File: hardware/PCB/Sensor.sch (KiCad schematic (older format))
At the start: 2 parts

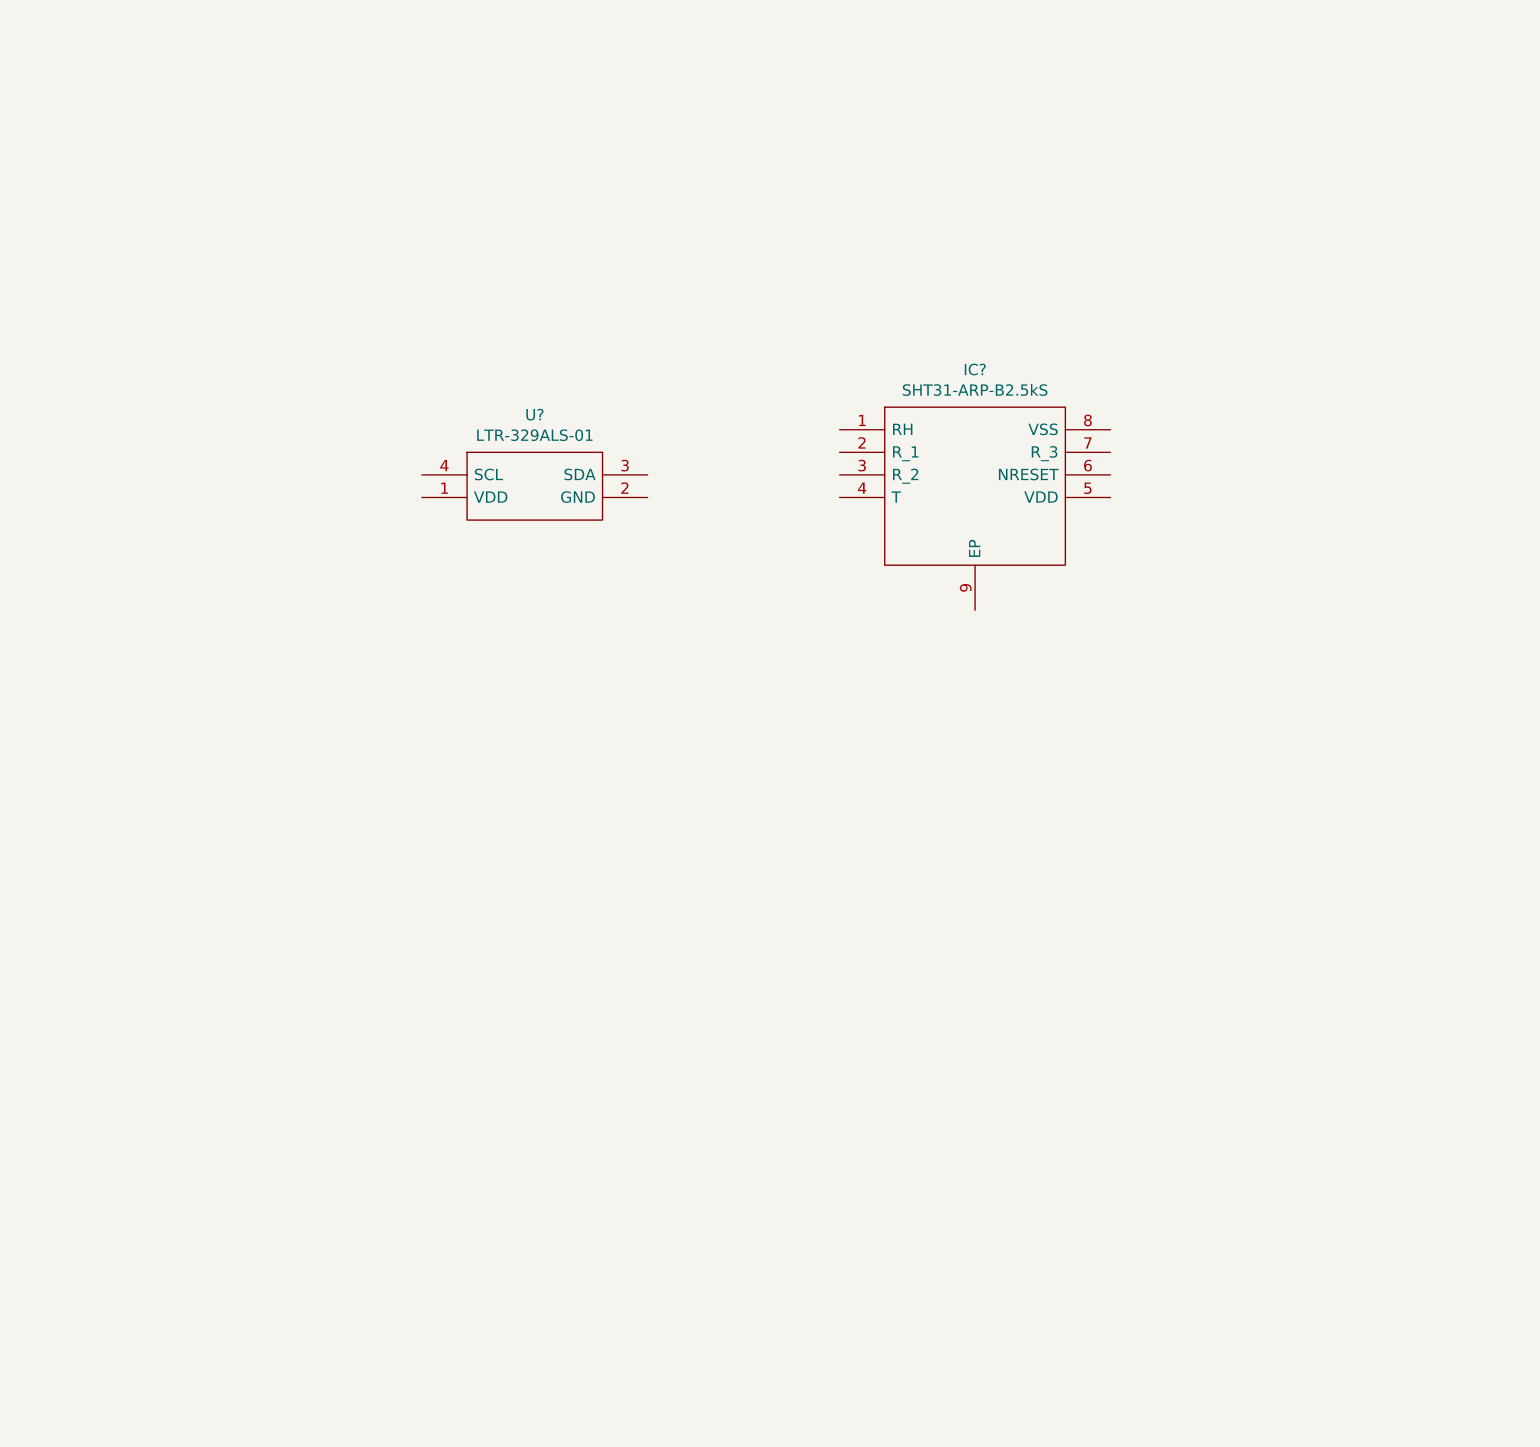
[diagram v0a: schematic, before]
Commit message: Complete Sensor schematic
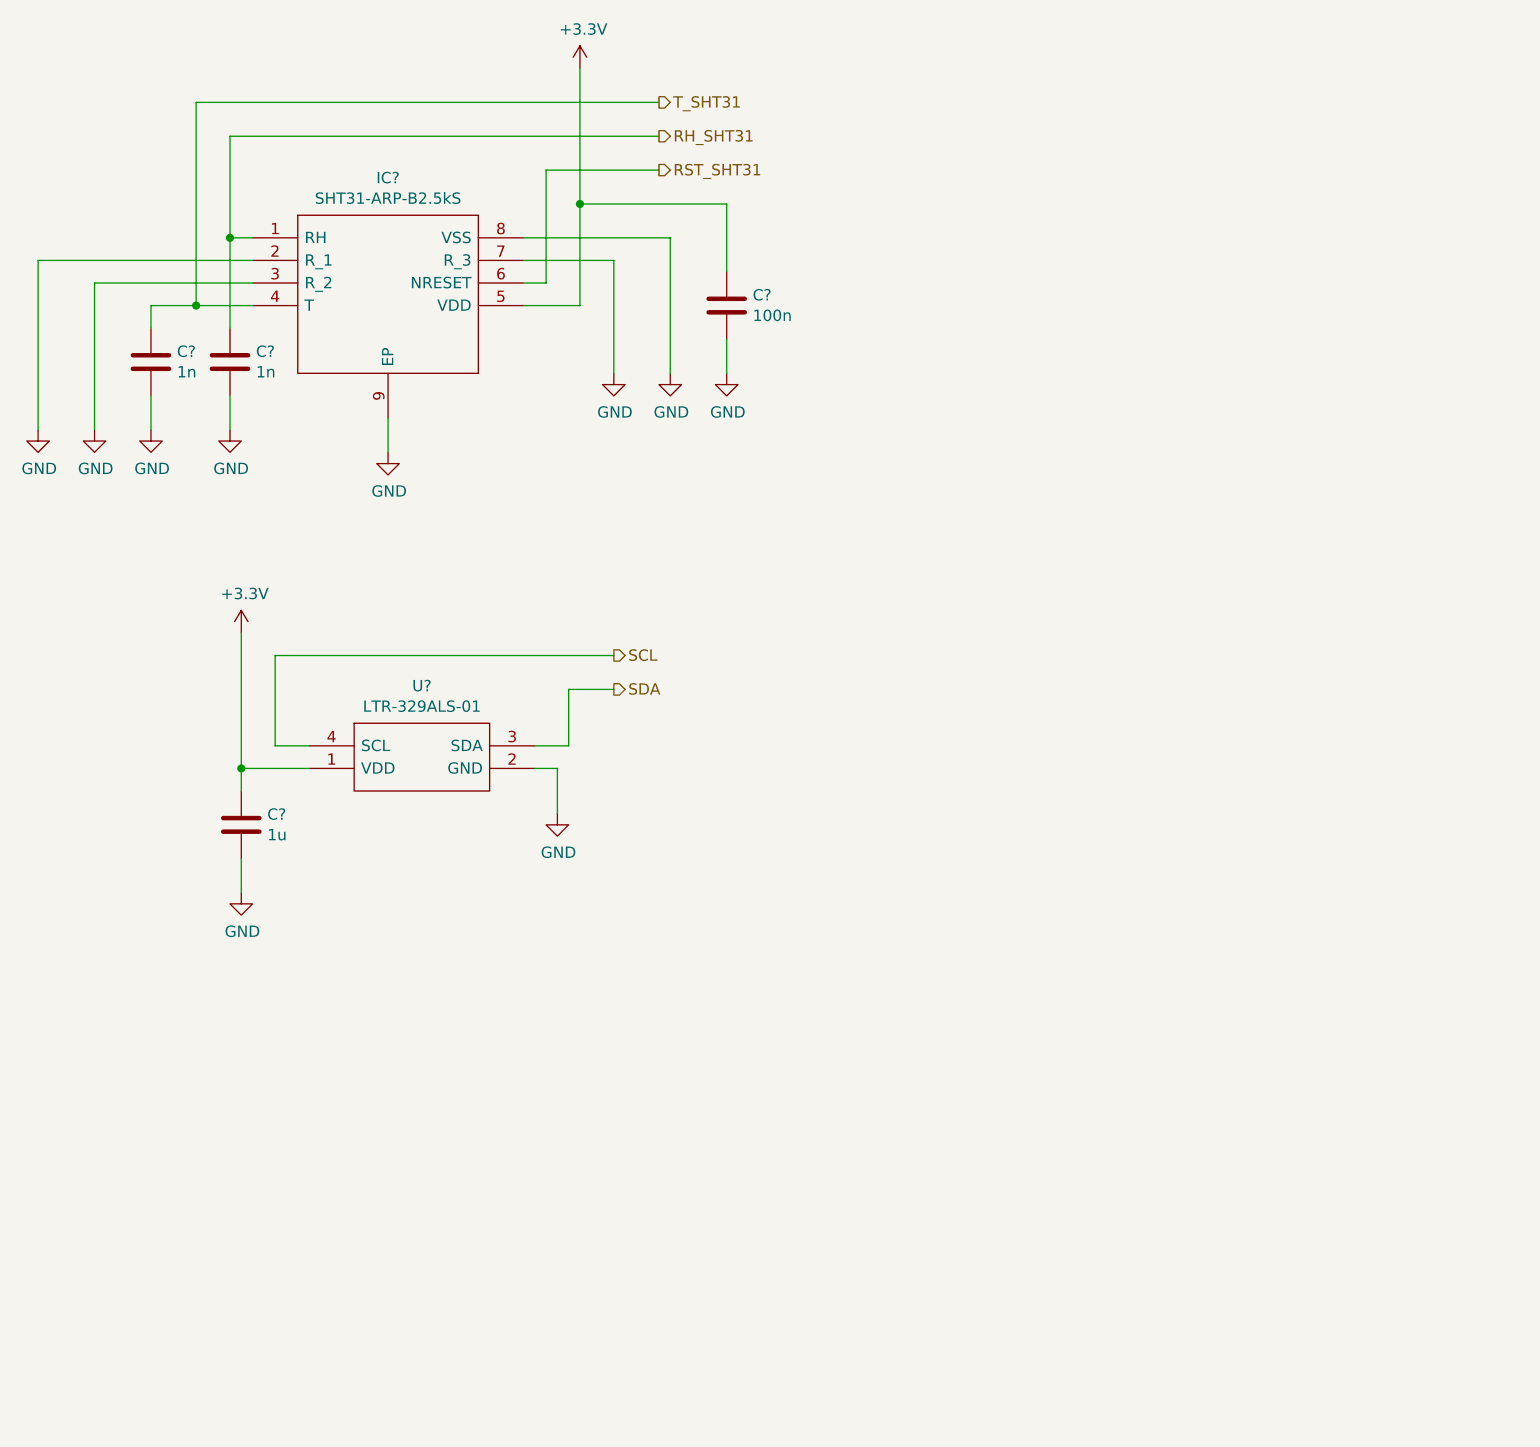
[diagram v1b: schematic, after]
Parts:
- added C?: 100n, symbol Device:C
- added C? (x2): 1n, symbol Device:C
- added C?: 1u, symbol Device:C
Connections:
- net +3V3: now reaches U?.1 (VDD)
- net +3V3: now also IC?.5 (VDD), C?.1, C?.1
- net GND: now reaches U?.2 (GND)
- net GND: now also IC?.2 (R_1), IC?.3 (R_2), IC?.7 (R_3), IC?.8 (VSS), IC?.9 (EP), C?.2, C?.2, C?.2, C?.2
- net SDA: now reaches U?.3 (SDA)
- net SCL: now reaches U?.4 (SCL)
- net RH_SHT31: now reaches IC?.1 (RH)
- net RH_SHT31: now also C?.1
- net T_SHT31: now reaches IC?.4 (T)
- net T_SHT31: now also C?.1
- net RST_SHT31: now reaches IC?.6 (NRESET)
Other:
- moved on the sheet: IC?, U?

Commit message: Add LPS22HD pressure sensor
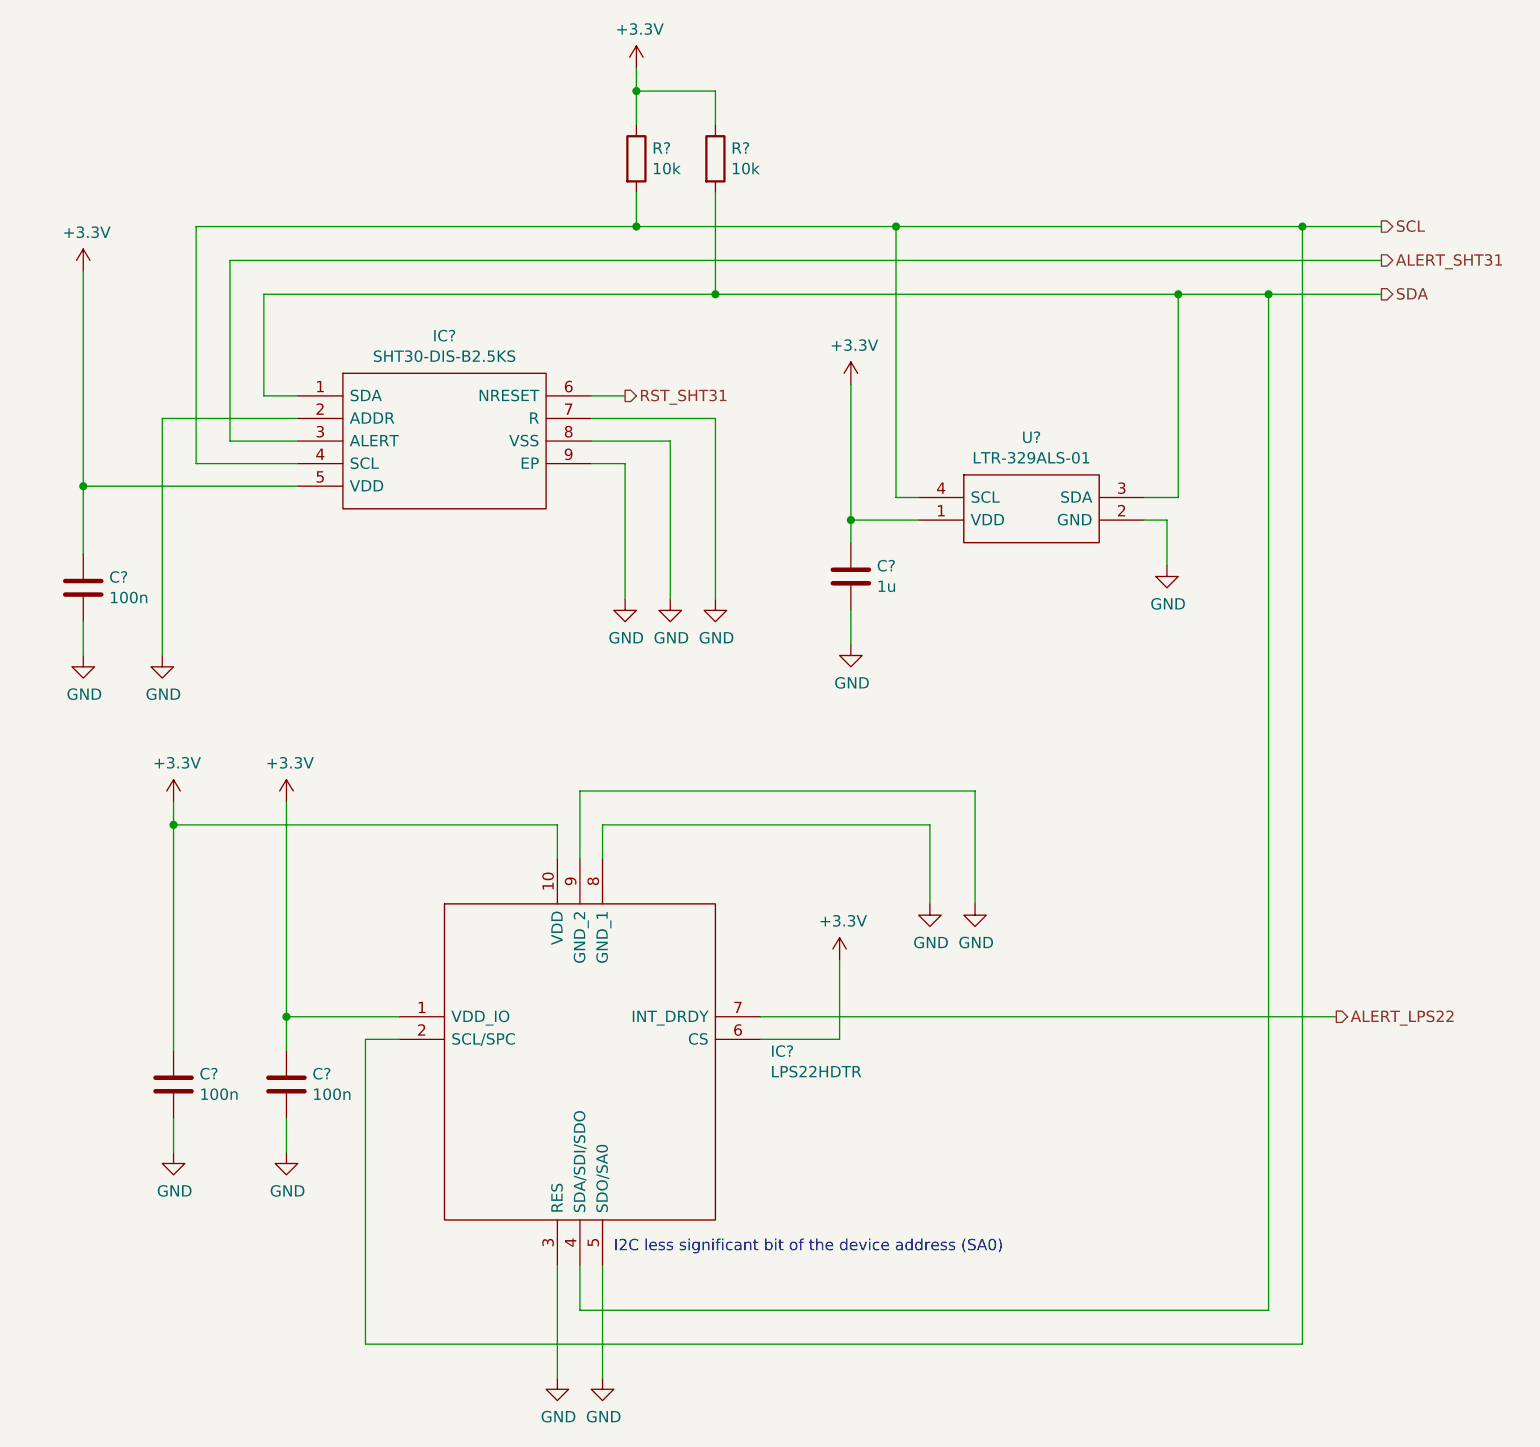
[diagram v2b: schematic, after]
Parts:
- removed C?: 100n, symbol Device:C
- removed C? (x2): 1n, symbol Device:C
- removed IC?: SHT31-ARP-B2.5kS, SON50P250X250X100-9N-D, symbol ProjectLibrary:SHT31-ARP-B2.5kS
- added C? (x3): 100n, symbol Device:C
- added IC?: SHT30-DIS-B2.5KS, SHT30DISB25KS, symbol ProjectLibrary:SHT30-DIS-B2.5KS
- added IC?: LPS22HDTR, LPS22HDTR, symbol ProjectLibrary:LPS22HDTR
- added R? (x2): 10k, symbol Device:R
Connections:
- net +3V3: now also C?.1, C?.1, C?.1, IC?.1 (VDD_IO), IC?.10 (VDD), IC?.5 (VDD), IC?.6 (CS), R?.1, R?.1
- net GND: now also C?.2, C?.2, C?.2, IC?.2 (ADDR), IC?.3 (RES), IC?.5 (SDO/SA0), IC?.7 (R), IC?.8 (GND_1), IC?.8 (VSS), IC?.9 (EP), IC?.9 (GND_2)
- net RST_SHT31: now also IC?.6 (NRESET)
- net SCL: now also IC?.2 (SCL/SPC), IC?.4 (SCL), R?.2
- net SDA: now also IC?.1 (SDA), IC?.4 (SDA/SDI/SDO), R?.2
- new net ALERT_LPS22: IC?.7 (INT_DRDY)
- new net ALERT_SHT31: IC?.3 (ALERT)
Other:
- note added: "I2C less significant bit of the device address (SA0)"
- moved on the sheet: C?, U?

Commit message: add 10k pull up
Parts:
- added R? (x3): 10k, symbol Device:R
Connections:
- net +3V3: now also R?.1, R?.1, R?.1
- net ALERT_LPS22: now also R?.2
- net ALERT_SHT31: now also R?.2
- net RST_SHT31: now also R?.2
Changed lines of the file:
@@
 Text HLabel 3350 2300 2    50   Output ~ 0
 RST_SHT31
-Wire Wire Line
-	3200 2300 3350 2300
 Text HLabel 6700 1550 2    50   Output ~ 0
 SCL
@@
 Connection ~ 4550 1550
 Wire Wire Line
-	4550 1550 6350 1550
-Wire Wire Line
-	1600 1700 6700 1700
+	1600 1700 6200 1700
 Wire Wire Line
 	3750 1850 5800 1850
@@
 ALERT_LPS22
 Wire Wire Line
-	3950 5050 6500 5050
+	3950 5050 5750 5050
+$Comp
+L Device:R R?
+U 1 1 5FD8C795
+P 3100 1250
+F 0 "R?" H 3170 1296 50  0000 L CNN
+F 1 "10k" H 3170 1205 50  0000 L CNN
+F 2 "" V 3030 1250 50  0001 C CNN
+F 3 "~" H 3100 1250 50  0001 C CNN
+	1    3100 1250
+	1    0    0    -1
+$EndComp
+$Comp
+L Device:R R?
+U 1 1 5FD8E1C7
+P 6200 1300
+F 0 "R?" H 6270 1346 50  0000 L CNN
+F 1 "10k" H 6270 1255 50  0000 L CNN
+F 2 "" V 6130 1300 50  0001 C CNN
+F 3 "~" H 6200 1300 50  0001 C CNN
+	1    6200 1300
+	1    0    0    -1
+$EndComp
+$Comp
+L Device:R R?
+U 1 1 5FD8FA02
+P 5750 4800
+F 0 "R?" H 5820 4846 50  0000 L CNN
+F 1 "10k" H 5820 4755 50  0000 L CNN
+F 2 "" V 5680 4800 50  0001 C CNN
+F 3 "~" H 5750 4800 50  0001 C CNN
+	1    5750 4800
+	1    0    0    -1
+$EndComp
+Wire Wire Line
+	4550 1550 6350 1550
+Wire Wire Line
+	3200 2300 3300 2300
+Wire Wire Line
+	3100 950  3400 950
+Wire Wire Line
+	3100 950  3100 1100
+Wire Wire Line
+	3100 1400 3100 2000
+Wire Wire Line
+	3100 2000 3300 2000
+Wire Wire Line
+	3300 2000 3300 2300
+Connection ~ 3300 2300
+Wire Wire Line
+	3300 2300 3350 2300
+Wire Wire Line
+	6200 1450 6200 1700
+Connection ~ 6200 1700
+Wire Wire Line
+	6200 1700 6700 1700
+$Comp
+L power:+3.3V #PWR?
+U 1 1 5FDA12EA
+P 6200 1000
+F 0 "#PWR?" H 6200 850 50  0001 C CNN
+F 1 "+3.3V" H 6215 1173 50  0000 C CNN
+F 2 "" H 6200 1000 50  0001 C CNN
+F 3 "" H 6200 1000 50  0001 C CNN
+	1    6200 1000
+	1    0    0    -1
+$EndComp
+Wire Wire Line
+	6200 1150 6200 1000
+$Comp
+L power:+3.3V #PWR?
+U 1 1 5FDA564B
+P 5750 4500
+F 0 "#PWR?" H 5750 4350 50  0001 C CNN
+F 1 "+3.3V" H 5765 4673 50  0000 C CNN
+F 2 "" H 5750 4500 50  0001 C CNN
+F 3 "" H 5750 4500 50  0001 C CNN
+	1    5750 4500
+	1    0    0    -1
+$EndComp
+Wire Wire Line
+	5750 4500 5750 4650
+Wire Wire Line
+	5750 4950 5750 5050
+Connection ~ 5750 5050
+Wire Wire Line
+	5750 5050 6500 5050
 $EndSCHEMATC
